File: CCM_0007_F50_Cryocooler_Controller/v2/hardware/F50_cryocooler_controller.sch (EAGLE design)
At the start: 50 parts, among them IC1 74LVC1G79DBV, IC2 MCP601OT, Q2 IRLL024, Q3 IRLL024, U1 MAX4466EXK+T, U3 PHOTON_WITH_HEADERS, X2 BNCPTH

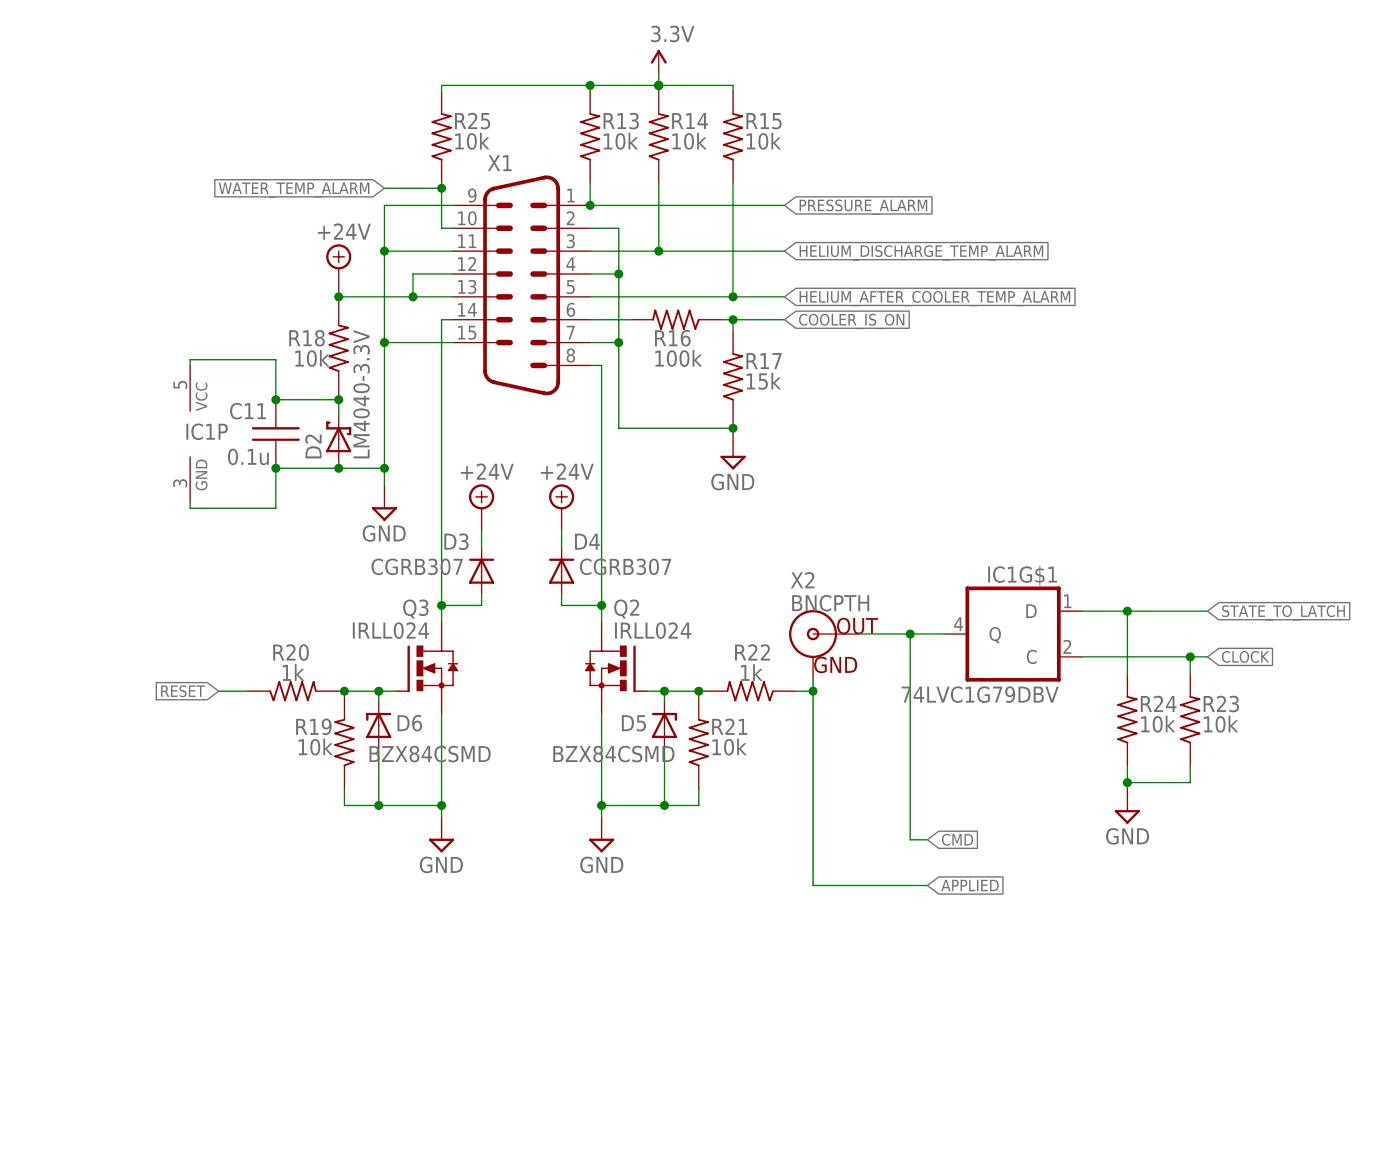
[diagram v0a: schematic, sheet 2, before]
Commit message: CCM_0007: finished layout of v2.
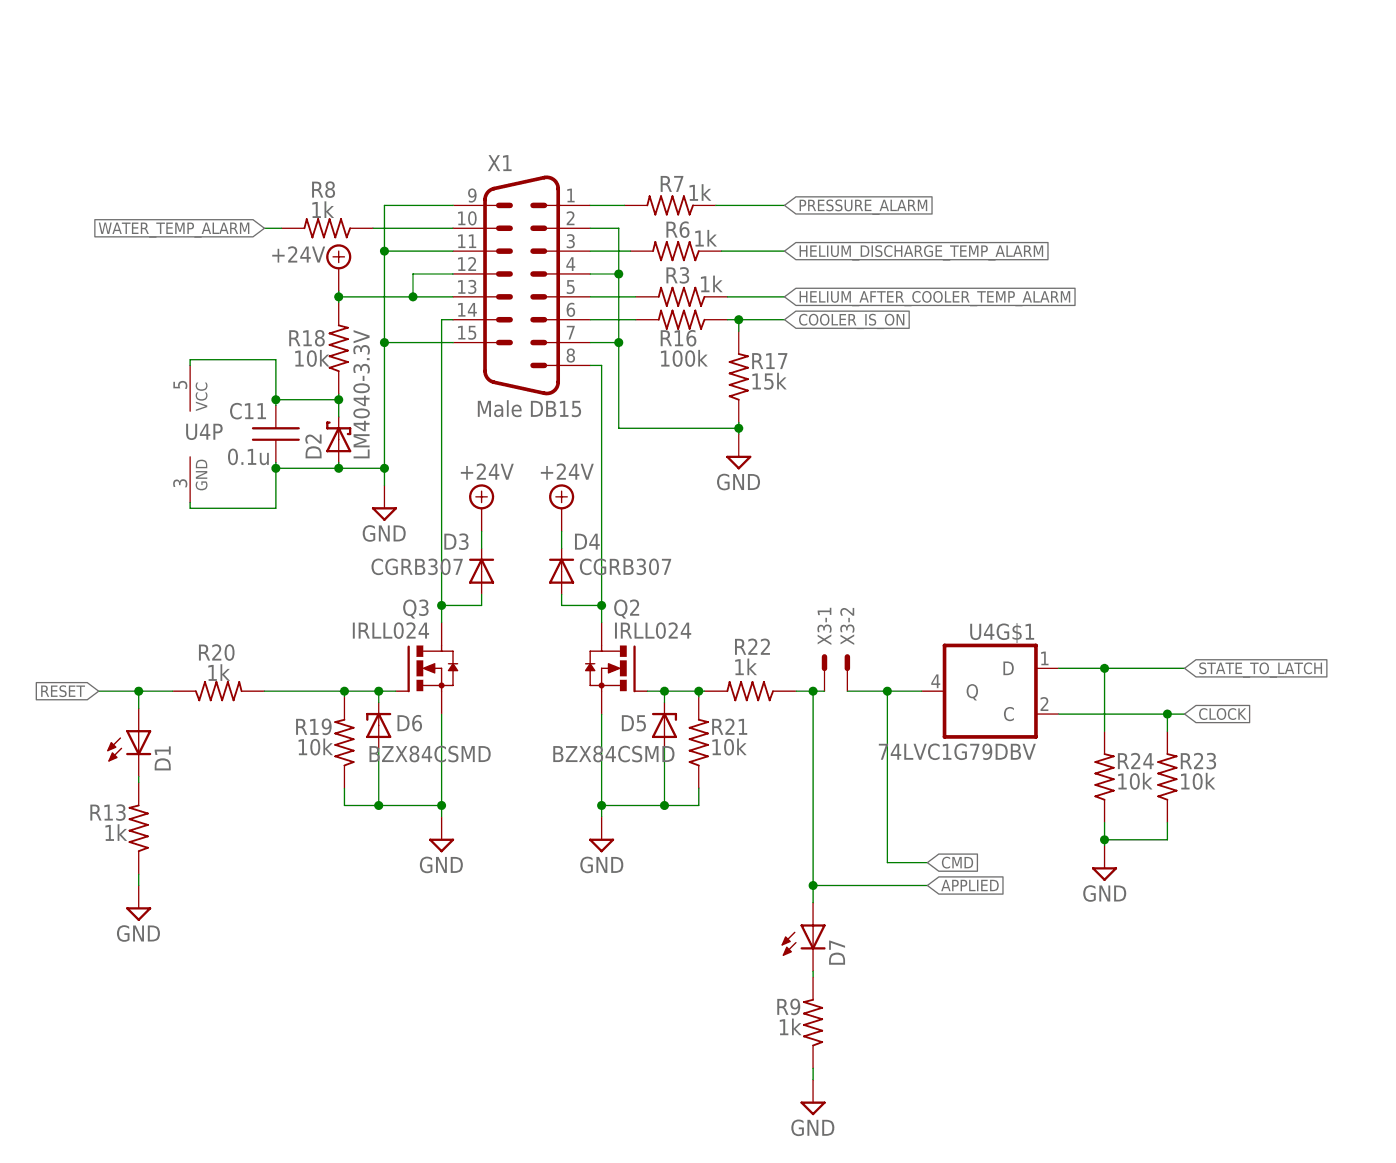
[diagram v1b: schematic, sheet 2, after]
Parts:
- removed R14, R15, R25: 10k, acrooptics:R0603
- removed U$1: BNCPTH, SparkFun:BNCPTH
- added D1, D7: (no value), acrooptics:LED0603
- added R3, R6, R7, R8, R9: 1k, acrooptics:R0603
- added X3: 22-23-2021, con-molex:22-23-2021
- R13: value 10k -> 1k
- X1: value (none) -> Male DB15
- renumbered IC1 to U4, IC2 to U2, U$2 to X5, U$3 to X4
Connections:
- new net N$12: R6.2, X1.3
- new net N$16: R3.2, X1.5
- new net N$17: D1.C, R13.2
- new net N$18: D7.C, R9.2
- new net N$6: R8.1, X1.10
- new net N$9: R7.2, X1.1
- net 3.3V: no longer R13.2, R14.2, R15.2, R25.2
- net APPLIED: now also D7.A, X3-1.S; no longer X2.GND
- net CMD: now also X3-2.S; no longer X2.OUT
- net GND: now also R13.1, R9.1, X2.GND; no longer U$1.GND
- net HELIUM_AFTER_COOLER_TEMP_ALARM: now also R3.1; no longer R15.1, X1.5
- net HELIUM_DISCHARGE_TEMP_ALARM: now also R6.1; no longer R14.1, X1.3
- net PRESSURE_ALARM: now also R7.1; no longer R13.1, X1.1
- net RESET: now also D1.A
- net SYNC_OUT: now also X2.OUT; no longer U$1.OUT
- net WATER_TEMP_ALARM: now also R8.2; no longer R25.1, X1.10
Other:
- note added: "100 mA max load"
- note added: "circuit powered from on-board Photon regulator which gets 5V from USB connection use internal pullups / pulldowns"
- note added: "use Photon pullups for alarm signals"
- note added: "vacuum interlock jump to ignore"
- note removed: "BNC to pressure interlock closes when vacuum jump to ignore"
- note removed: "circuit powered from on-board Photon regulator which gets 5V from USB connection"
- moved on the sheet: R13, R16, R17, R20, R23, R24
